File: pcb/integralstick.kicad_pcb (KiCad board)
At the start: 4 copper layers, 9 parts, among them J1 CONN_INTEGRALSTICK_FPGA_DEVICE, J2 CONN_INTEGRALSTICK_MCU_DEVICE, U1 STM32F777NIH6‎, U2 XC7A50T-1FTG256C, U3 S27KS0641, U4 S27KS0641, U5 KSZ9031RN, U6 S25FL064LABNFI011‎, U7 LTC3374-QFN

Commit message: Finished initial schematic. Pin assignments will likely change during routing. Ready for test point insertion and signoff review.
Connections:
- net Net-(U5-Pad1) renamed /Ethernet/A2V5
- net Net-(U5-Pad14) renamed /1V2
- net Net-(U5-Pad4) renamed /Ethernet/A1V2
- J1 pad 1: /Power Supply/1V8 -> /1V8
- J1 pad 100: /Power Supply/3V3 -> /3V3
- J1 pad 101: /FPGA/IO_3V3_18 -> /FPGA/IO_3V3_16
- J1 pad 102: /FPGA/IO_3V3_19 -> /FPGA/IO_3V3_17
- J1 pad 103: /FPGA/IO_3V3_20 -> /FPGA/IO_3V3_18
- J1 pad 104: /FPGA/IO_3V3_21 -> /FPGA/IO_3V3_19
- J1 pad 105: /Power Supply/3V3 -> /3V3
- J1 pad 106: /Power Supply/3V3 -> /3V3
- J1 pad 107: /FPGA/IO_3V3_22 -> /FPGA/IO_3V3_20
- J1 pad 108: /FPGA/IO_3V3_23 -> /FPGA/IO_3V3_21
- J1 pad 109: /FPGA/IO_3V3_24 -> /FPGA/IO_3V3_22
- J1 pad 110: /FPGA/IO_3V3_25 -> /FPGA/IO_3V3_23
- J1 pad 111: /Power Supply/3V3 -> /3V3
- J1 pad 112: /Power Supply/3V3 -> /3V3
- J1 pad 113: /FPGA/IO_3V3_26 -> /FPGA/IO_3V3_24
- J1 pad 114: /FPGA/IO_3V3_27 -> /FPGA/IO_3V3_25
- J1 pad 115: /FPGA/IO_3V3_28 -> /FPGA/IO_3V3_26
- J1 pad 116: /FPGA/IO_3V3_29 -> /FPGA/IO_3V3_27
- J1 pad 117: /Power Supply/3V3 -> /3V3
- J1 pad 118: /Power Supply/3V3 -> /3V3
- J1 pad 119: /FPGA/IO_3V3_30 -> /FPGA/IO_3V3_28
- J1 pad 120: /FPGA/IO_3V3_31 -> /FPGA/IO_3V3_29
- J1 pad 121: /Power Supply/GND -> /1V8
- J1 pad 122: /Power Supply/GND -> /1V8
- J1 pad 123: /Power Supply/GND -> /1V8
- J1 pad 124: /Power Supply/GND -> /1V8
- J1 pad 125: /Power Supply/GND -> /1V8
- J1 pad 126: /Power Supply/GND -> /1V8
- J1 pad 127: /Power Supply/GND -> /1V8
- J1 pad 128: /Power Supply/GND -> /1V8
- J1 pad 13: /Power Supply/1V8 -> /1V8
- J1 pad 14: /Power Supply/1V8 -> /1V8
- J1 pad 19: /Power Supply/1V8 -> /1V8
- J1 pad 2: /Power Supply/1V8 -> /1V8
- J1 pad 20: /Power Supply/1V8 -> /1V8
- J1 pad 25: /Power Supply/1V8 -> /1V8
- J1 pad 26: /Power Supply/1V8 -> /1V8
- J1 pad 31: /Power Supply/1V8 -> /1V8
- J1 pad 32: /Power Supply/1V8 -> /1V8
- J1 pad 69: /Power Supply/3V3 -> /3V3
- J1 pad 7: /Power Supply/1V8 -> /1V8
- J1 pad 70: /Power Supply/3V3 -> /3V3
- J1 pad 75: /Power Supply/3V3 -> /3V3
- J1 pad 76: /Power Supply/3V3 -> /3V3
- J1 pad 78: /FPGA/IO_3V3_3 -> /FPGA/IN_3V3_0_P
- J1 pad 79: /FPGA/IO_3V3_4 -> /FPGA/IO_3V3_3
- J1 pad 8: /Power Supply/1V8 -> /1V8
- J1 pad 80: /FPGA/IO_3V3_5 -> /FPGA/IN_3V3_0_N
- J1 pad 81: /Power Supply/3V3 -> /3V3
- J1 pad 82: /Power Supply/3V3 -> /3V3
- J1 pad 83: /FPGA/IO_3V3_6 -> /FPGA/IO_3V3_4
- J1 pad 84: /FPGA/IO_3V3_7 -> /FPGA/IO_3V3_5
- J1 pad 85: /FPGA/IO_3V3_8 -> /FPGA/IO_3V3_6
- J1 pad 86: /FPGA/IO_3V3_9 -> /FPGA/IO_3V3_7
- J1 pad 87: /Power Supply/3V3 -> /3V3
- J1 pad 88: /Power Supply/3V3 -> /3V3
- J1 pad 89: /FPGA/IO_3V3_10 -> /FPGA/IO_3V3_8
- J1 pad 90: /FPGA/IO_3V3_11 -> /FPGA/IO_3V3_9
- J1 pad 91: /FPGA/IO_3V3_12 -> /FPGA/IO_3V3_10
- J1 pad 92: /FPGA/IO_3V3_13 -> /FPGA/IO_3V3_11
- J1 pad 93: /Power Supply/3V3 -> /3V3
- J1 pad 94: /Power Supply/3V3 -> /3V3
- J1 pad 95: /FPGA/IO_3V3_14 -> /FPGA/IO_3V3_12
- J1 pad 96: /FPGA/IO_3V3_15 -> /FPGA/IO_3V3_13
- J1 pad 97: /FPGA/IO_3V3_16 -> /FPGA/IO_3V3_14
- J1 pad 98: /FPGA/IO_3V3_17 -> /FPGA/IO_3V3_15
- J1 pad 99: /Power Supply/3V3 -> /3V3
- J2 pad 1: (no net) -> /3V3
- J2 pad 10: (no net) -> /FPGA_RST_N
- J2 pad 103: (no net) -> /3V3
- J2 pad 104: (no net) -> /3V3
- J2 pad 109: /Power Supply/GND -> /1V8
- J2 pad 11: (no net) -> /FPGA_DONE
- J2 pad 110: /Power Supply/GND -> /1V8
- J2 pad 115: /Power Supply/GND -> /1V8
- J2 pad 116: /Power Supply/GND -> /1V8
- J2 pad 12: (no net) -> Net-(J2-Pad12)
- J2 pad 121: /Power Supply/GND -> /1V8
- J2 pad 122: /Power Supply/GND -> /1V8
- J2 pad 123: /Power Supply/GND -> /1V8
- J2 pad 124: /Power Supply/GND -> /1V8
- J2 pad 125: /Power Supply/GND -> /1V8
- J2 pad 126: /Power Supply/GND -> /1V8
- J2 pad 127: /Power Supply/GND -> /1V8
- J2 pad 128: /Power Supply/GND -> /1V8
- J2 pad 13: (no net) -> /3V3
- J2 pad 14: (no net) -> /3V3
- J2 pad 19: (no net) -> /3V3
- J2 pad 2: (no net) -> /3V3
- J2 pad 20: (no net) -> /3V3
- J2 pad 25: (no net) -> /3V3
- J2 pad 26: (no net) -> /3V3
- J2 pad 3: (no net) -> /FPGA_TDI
- J2 pad 31: (no net) -> /3V3
- J2 pad 32: (no net) -> /3V3
- J2 pad 37: (no net) -> /3V3
- J2 pad 38: (no net) -> /3V3
- J2 pad 4: (no net) -> /JTAG_TMS
- J2 pad 43: (no net) -> /3V3
- J2 pad 44: (no net) -> /3V3
- J2 pad 49: (no net) -> /3V3
- J2 pad 5: (no net) -> /JTAG_TCK
- J2 pad 50: (no net) -> /3V3
- J2 pad 55: (no net) -> /3V3
- J2 pad 56: (no net) -> /3V3
- J2 pad 6: (no net) -> /MCU_TDO
- J2 pad 61: (no net) -> /3V3
- J2 pad 62: (no net) -> /3V3
- J2 pad 67: (no net) -> /3V3
- J2 pad 68: (no net) -> /3V3
- J2 pad 7: (no net) -> /3V3
- J2 pad 73: (no net) -> /3V3
- J2 pad 74: (no net) -> /3V3
- J2 pad 79: (no net) -> /3V3
- J2 pad 8: (no net) -> /3V3
- J2 pad 80: (no net) -> /3V3
- J2 pad 85: (no net) -> /3V3
- J2 pad 86: (no net) -> /3V3
- J2 pad 9: (no net) -> /MCU_RST_N
- J2 pad 91: (no net) -> /3V3
- J2 pad 92: (no net) -> /3V3
- J2 pad 97: (no net) -> /3V3
- J2 pad 98: (no net) -> /3V3
- U1 pad A10: (no net) -> /MCU_TDO
- U1 pad A13: (no net) -> /FPGA_TDO
- U1 pad A14: (no net) -> /JTAG_TCK
- U1 pad A15: (no net) -> /JTAG_TMS
- U1 pad A4: (no net) -> Net-(U1-PadA4)
- U1 pad B10: (no net) -> Net-(U1-PadB10)
- U1 pad B3: (no net) -> Net-(U1-PadB3)
- U1 pad B7: (no net) -> Net-(U1-PadB7)
- U1 pad B8: (no net) -> Net-(U1-PadB8)
- U1 pad B9: (no net) -> Net-(U1-PadB9)
- U1 pad C1: (no net) -> /3V3
- U1 pad C13: (no net) -> Net-(U1-PadC13)
- U1 pad C14: (no net) -> Net-(U1-PadC14)
- U1 pad C2: (no net) -> Net-(U1-PadC2)
- U1 pad C3: (no net) -> Net-(U1-PadC3)
- U1 pad C4: (no net) -> Net-(U1-PadC4)
- U1 pad C5: (no net) -> Net-(U1-PadC5)
- U1 pad C6: (no net) -> Net-(U1-PadC6)
- U1 pad C7: (no net) -> Net-(U1-PadC7)
- U1 pad C8: (no net) -> Net-(U1-PadC8)
- U1 pad C9: (no net) -> Net-(U1-PadC9)
- U1 pad D10: (no net) -> Net-(U1-PadD10)
- U1 pad D13: (no net) -> Net-(U1-PadD13)
- U1 pad D14: (no net) -> Net-(U1-PadD14)
- U1 pad D3: (no net) -> Net-(U1-PadD3)
- U1 pad D4: (no net) -> Net-(U1-PadD4)
- U1 pad D5: (no net) -> Net-(U1-PadD5)
- U1 pad D6: (no net) -> Net-(U1-PadD6)
- U1 pad D7: (no net) -> Net-(U1-PadD7)
- U1 pad D8: (no net) -> Net-(U1-PadD8)
- U1 pad D9: (no net) -> Net-(U1-PadD9)
- U1 pad E1: (no net) -> /MCU/CLK_32KHZ
- U1 pad E10: /Power Supply/3V3 -> /3V3
- U1 pad E11: (no net) -> Net-(C2-Pad1)
- U1 pad E12: (no net) -> Net-(U1-PadE12)
- U1 pad E13: (no net) -> Net-(U1-PadE13)
- U1 pad E14: (no net) -> Net-(U1-PadE14)
- U1 pad E3: (no net) -> Net-(U1-PadE3)
- U1 pad E4: (no net) -> Net-(U1-PadE4)
- U1 pad E5: (no net) -> /3V3
- U1 pad E6: (no net) -> /1V8
- U1 pad E7: /Power Supply/3V3 -> /3V3
- U1 pad E8: /Power Supply/3V3 -> /3V3
- U1 pad E9: (no net) -> /3V3
- U1 pad F1: (no net) -> Net-(U1-PadF1)
- U1 pad F10: /Power Supply/GND -> /1V8
- U1 pad F11: /Power Supply/3V3 -> /3V3
- U1 pad F12: (no net) -> Net-(U1-PadF12)
- U1 pad F13: (no net) -> Net-(U1-PadF13)
- U1 pad F2: /Power Supply/GND -> /1V8
- U1 pad F3: (no net) -> Net-(U1-PadF3)
- U1 pad F4: /Power Supply/3V3 -> /3V3
- U1 pad F5: /Power Supply/3V3 -> /3V3
- U1 pad F6: /Power Supply/GND -> /1V8
- U1 pad F7: /Power Supply/GND -> /1V8
- U1 pad F8: /Power Supply/GND -> /1V8
- U1 pad F9: /Power Supply/GND -> /1V8
- U1 pad G1: (no net) -> /MCU/MCU_CLK_25MHZ
- U1 pad G10: /Power Supply/GND -> /1V8
- U1 pad G11: (no net) -> /3V3
- U1 pad G12: (no net) -> Net-(U1-PadG12)
- U1 pad G13: (no net) -> Net-(U1-PadG13)
- U1 pad G3: (no net) -> Net-(U1-PadG3)
- U1 pad G4: (no net) -> Net-(U1-PadG4)
- U1 pad G5: /Power Supply/3V3 -> /3V3
- U1 pad G6: /Power Supply/GND -> /1V8
- U1 pad H1: (no net) -> Net-(U1-PadH1)
- U1 pad H10: /Power Supply/GND -> /1V8
- U1 pad H11: /Power Supply/3V3 -> /3V3
- U1 pad H12: (no net) -> Net-(U1-PadH12)
- U1 pad H13: (no net) -> Net-(U1-PadH13)
- U1 pad H14: (no net) -> Net-(U1-PadH14)
- U1 pad H3: (no net) -> Net-(U1-PadH3)
- U1 pad H4: (no net) -> Net-(U1-PadH4)
- U1 pad H5: /Power Supply/3V3 -> /3V3
- U1 pad H6: /Power Supply/GND -> /1V8
- U1 pad J1: (no net) -> /MCU_RST_N
- U1 pad J10: /Power Supply/GND -> /1V8
- U1 pad J11: /Power Supply/3V3 -> /3V3
- U1 pad J12: (no net) -> Net-(U1-PadJ12)
- U1 pad J13: (no net) -> Net-(U1-PadJ13)
- U1 pad J14: (no net) -> Net-(U1-PadJ14)
- U1 pad J15: (no net) -> Net-(U1-PadJ15)
- U1 pad J3: (no net) -> Net-(U1-PadJ3)
- U1 pad J4: (no net) -> Net-(U1-PadJ4)
- U1 pad J5: /Power Supply/3V3 -> /3V3
- U1 pad J6: /Power Supply/GND -> /1V8
- U1 pad K10: /Power Supply/GND -> /1V8
- U1 pad K11: /Power Supply/3V3 -> /3V3
- U1 pad K12: (no net) -> Net-(U1-PadK12)
- U1 pad K4: (no net) -> Net-(U1-PadK4)
- U1 pad K5: /Power Supply/3V3 -> /3V3
- U1 pad K6: /Power Supply/GND -> /1V8
- U1 pad K7: /Power Supply/GND -> /1V8
- U1 pad K8: /Power Supply/GND -> /1V8
- U1 pad K9: /Power Supply/GND -> /1V8
- U1 pad L1: (no net) -> Net-(U1-PadL1)
- U1 pad L10: /Power Supply/3V3 -> /3V3
- U1 pad L11: (no net) -> Net-(C1-Pad2)
- U1 pad L5: (no net) -> /1V8
- U1 pad L6: /Power Supply/GND -> /1V8
- U1 pad L7: /Power Supply/3V3 -> /3V3
- U1 pad L8: /Power Supply/3V3 -> /3V3
- U1 pad L9: /Power Supply/3V3 -> /3V3
- U1 pad M1: /Power Supply/GND -> /1V8
- U1 pad M12: (no net) -> Net-(U1-PadM12)
- U1 pad M13: (no net) -> Net-(U1-PadM13)
- U1 pad M14: (no net) -> Net-(U1-PadM14)
- U1 pad M15: (no net) -> Net-(U1-PadM15)
- U1 pad M6: (no net) -> Net-(U1-PadM6)
- U1 pad M7: (no net) -> Net-(U1-PadM7)
- U1 pad M8: (no net) -> Net-(U1-PadM8)
- U1 pad M9: (no net) -> Net-(U1-PadM9)
- U1 pad N1: (no net) -> /1V8
- U1 pad N11: (no net) -> Net-(U1-PadN11)
- U1 pad N12: (no net) -> Net-(U1-PadN12)
- U1 pad N13: (no net) -> Net-(U1-PadN13)
- U1 pad N14: (no net) -> Net-(U1-PadN14)
- U1 pad N15: (no net) -> Net-(U1-PadN15)
- U1 pad N6: (no net) -> Net-(U1-PadN6)
- U1 pad N7: (no net) -> Net-(U1-PadN7)
- U1 pad N8: (no net) -> Net-(U1-PadN8)
- U1 pad P1: (no net) -> /3V3
- U1 pad P13: (no net) -> Net-(U1-PadP13)
- U1 pad P14: (no net) -> Net-(U1-PadP14)
- U1 pad P15: (no net) -> Net-(U1-PadP15)
- U1 pad P6: (no net) -> Net-(U1-PadP6)
- U1 pad P7: (no net) -> Net-(U1-PadP7)
- U1 pad P8: (no net) -> Net-(U1-PadP8)
- U1 pad R1: /Power Supply/3V3 -> /3V3
- U1 pad R6: (no net) -> Net-(U1-PadR6)
- U1 pad R7: (no net) -> Net-(U1-PadR7)
- U2 pad A1: /Power Supply/GND -> /1V8
- U2 pad A11: /Power Supply/GND -> /1V8
- U2 pad A16: /Power Supply/3V3 -> /3V3
- U2 pad A6: /Power Supply/1V8 -> /1V8
- U2 pad B13: /Power Supply/3V3 -> /3V3
- U2 pad B3: /Power Supply/1V8 -> /1V8
- U2 pad B8: /Power Supply/GND -> /1V8
- U2 pad C10: /Power Supply/3V3 -> /3V3
- U2 pad C15: /Power Supply/GND -> /1V8
- U2 pad C5: /Power Supply/GND -> /1V8
- U2 pad D12: /Power Supply/GND -> /1V8
- U2 pad D16: (no net) -> /FPGA/IN_3V3_0_N
- U2 pad D2: /Power Supply/GND -> /1V8
- U2 pad D7: /Power Supply/1V8 -> /1V8
- U2 pad E14: /Power Supply/3V3 -> /3V3
- U2 pad E15: (no net) -> Net-(U2-PadE15)
- U2 pad E16: /FPGA/IO_3V3_31 -> /FPGA/IN_3V3_0_P
- U2 pad E4: /Power Supply/1V8 -> /1V8
- U2 pad E7: (no net) -> /FPGA/3V3
- U2 pad E8: (no net) -> /QSPI_CLK
- U2 pad E9: /Power Supply/GND -> /1V8
- U2 pad F1: /Power Supply/1V8 -> /1V8
- U2 pad F10: /Power Supply/GND -> /1V8
- U2 pad F13: /FPGA/IO_3V3_30 -> Net-(U2-PadF13)
- U2 pad F14: (no net) -> Net-(U2-PadF14)
- U2 pad F15: (no net) -> Net-(U2-PadF15)
- U2 pad F16: /Power Supply/GND -> /1V8
- U2 pad F6: /Power Supply/GND -> /1V8
- U2 pad F8: (no net) -> /1V8
- U2 pad G10: Net-(U2-PadG10) -> /1V8
- U2 pad G11: (no net) -> Net-(U2-PadG11)
- U2 pad G12: (no net) -> Net-(U2-PadG12)
- U2 pad G13: /Power Supply/GND -> /1V8
- U2 pad G14: (no net) -> Net-(U2-PadG14)
- U2 pad G15: (no net) -> /FPGA/I2C_SDA
- U2 pad G16: (no net) -> Net-(U2-PadG16)
- U2 pad G3: /Power Supply/GND -> /1V8
- U2 pad G7: /Power Supply/GND -> /1V8
- U2 pad G8: (no net) -> /1V8
- U2 pad G9: /Power Supply/GND -> /1V8
- U2 pad H10: (no net) -> /FPGA_DONE
- U2 pad H11: (no net) -> Net-(U2-PadH11)
- U2 pad H12: (no net) -> Net-(U2-PadH12)
- U2 pad H13: (no net) -> Net-(U2-PadH13)
- U2 pad H14: (no net) -> /FPGA/I2C_SCL
- U2 pad H15: /Power Supply/3V3 -> /3V3
- U2 pad H16: (no net) -> Net-(U2-PadH16)
- U2 pad H6: /Power Supply/GND -> /1V8
- U2 pad H7: (no net) -> /FPGA/GND
- U2 pad H8: (no net) -> Net-(U2-PadH8)
- U2 pad J10: Net-(U2-PadG10) -> /1V8
- U2 pad J11: /Power Supply/GND -> /1V8
- U2 pad J12: /Power Supply/3V3 -> /3V3
- U2 pad J15: (no net) -> Net-(U2-PadJ15)
- U2 pad J16: (no net) -> Net-(U2-PadJ16)
- U2 pad J2: /Power Supply/1V8 -> /1V8
- U2 pad J7: (no net) -> Net-(U2-PadJ7)
- U2 pad J8: (no net) -> /FPGA/GND
- U2 pad J9: /Power Supply/GND -> /1V8
- U2 pad K10: (no net) -> /FPGA/FPGA_INIT
- U2 pad K11: Net-(U2-PadG10) -> /1V8
- U2 pad K12: (no net) -> Net-(U2-PadK12)
- U2 pad K14: /Power Supply/GND -> /1V8
- U2 pad K4: /Power Supply/GND -> /1V8
- U2 pad K6: /Power Supply/GND -> /1V8
- U2 pad K7: (no net) -> /FPGA/GND
- U2 pad K8: (no net) -> /FPGA/GND
- U2 pad L1: /Power Supply/GND -> /1V8
- U2 pad L10: Net-(U2-PadG10) -> /1V8
- U2 pad L11: /Power Supply/GND -> /1V8
- U2 pad L15: /MCU/3V3 -> /3V3
- U2 pad L16: /Power Supply/3V3 -> /3V3
- U2 pad L6: /Power Supply/3V3 -> /3V3
- U2 pad L7: (no net) -> /JTAG_TCK
- U2 pad L9: (no net) -> /FPGA_RST_N
- U2 pad M10: (no net) -> /FPGA/GND
- U2 pad M11: (no net) -> /FPGA/GND
- U2 pad M13: /Power Supply/3V3 -> /3V3
- U2 pad M7: (no net) -> /JTAG_TMS
- U2 pad M8: /Power Supply/GND -> /1V8
- U2 pad M9: (no net) -> /FPGA/3V3
- U2 pad N10: /Power Supply/3V3 -> /3V3
- U2 pad N15: /Power Supply/GND -> /1V8
- U2 pad N5: /Power Supply/GND -> /1V8
- U2 pad N7: (no net) -> /FPGA_TDI
- U2 pad N8: (no net) -> /FPGA_TDO
- U2 pad N9: (no net) -> Net-(U2-PadN9)
- U2 pad P11: (no net) -> /ETH_LED1_N
- U2 pad P12: /Power Supply/GND -> /1V8
- U2 pad P2: /Power Supply/GND -> /1V8
- U2 pad P7: /Power Supply/3V3 -> /3V3
- U2 pad R10: (no net) -> Net-(U2-PadR10)
- U2 pad R11: (no net) -> Net-(U2-PadR11)
- U2 pad R12: (no net) -> /ETH_LED2_N
- U2 pad R13: (no net) -> Net-(U2-PadR13)
- U2 pad R14: /Power Supply/3V3 -> /3V3
- U2 pad R9: /Power Supply/GND -> /1V8
- U2 pad T11: /Power Supply/3V3 -> /3V3
- U2 pad T12: (no net) -> Net-(U2-PadT12)
- U2 pad T13: (no net) -> Net-(U2-PadT13)
- U2 pad T16: /Power Supply/GND -> /1V8
- U2 pad T6: /Power Supply/GND -> /1V8
- U3 pad B3: /RAM/GND -> /1V8
- U3 pad B4: /RAM/1V8 -> /1V8
- U3 pad C1: /RAM/GND -> /1V8
- U3 pad D1: /RAM/1V8 -> /1V8
- U3 pad E4: /RAM/1V8 -> /1V8
- U3 pad E5: /RAM/GND -> /1V8
- U4 pad B3: /RAM/GND -> /1V8
- U4 pad B4: /RAM/1V8 -> /1V8
- U4 pad C1: /RAM/GND -> /1V8
- U4 pad D1: /RAM/1V8 -> /1V8
- U4 pad E4: /RAM/1V8 -> /1V8
- U4 pad E5: /RAM/GND -> /1V8
- U5 pad 13: (no net) -> Net-(U5-Pad13)
- U5 pad 15: (no net) -> /ETH_LED2_N
- U5 pad 16: Net-(U5-Pad16) -> /3V3
- U5 pad 17: (no net) -> /ETH_LED1_N
- U5 pad 29: Net-(U5-Pad29) -> /1V8
- U5 pad 34: Net-(U5-Pad16) -> /3V3
- U5 pad 38: (no net) -> Net-(U5-Pad38)
- U5 pad 40: Net-(U5-Pad16) -> /3V3
- U5 pad 41: (no net) -> Net-(R5-Pad2)
- U5 pad 43: (no net) -> Net-(U5-Pad43)
- U5 pad 44: (no net) -> /Ethernet/A1V2_PLL
- U5 pad 45: (no net) -> Net-(U5-Pad45)
- U5 pad 46: (no net) -> /Ethernet/ETH_CLK_25MHZ
- U5 pad 47: (no net) -> Net-(U5-Pad47)
- U5 pad 48: (no net) -> Net-(R2-Pad2)
- U5 pad PAD: Net-(U5-Pad29) -> /1V8
- U6 pad 4: (no net) -> /1V8
- U6 pad 6: (no net) -> /QSPI_CLK
- U6 pad 8: /MCU/3V3 -> /3V3
- U7 pad 1: (no net) -> Net-(U7-Pad1)
- U7 pad 10: (no net) -> Net-(U7-Pad10)
- U7 pad 11: (no net) -> Net-(U7-Pad11)
- U7 pad 12: (no net) -> Net-(U7-Pad12)
- U7 pad 13: (no net) -> Net-(U7-Pad13)
- U7 pad 14: (no net) -> Net-(U7-Pad14)
- U7 pad 15: (no net) -> Net-(U7-Pad15)
- U7 pad 16: (no net) -> Net-(U7-Pad16)
- U7 pad 17: (no net) -> Net-(U7-Pad17)
- U7 pad 18: (no net) -> Net-(U7-Pad18)
- U7 pad 19: (no net) -> Net-(U7-Pad19)
- U7 pad 2: (no net) -> Net-(U7-Pad2)
- U7 pad 20: (no net) -> Net-(U7-Pad20)
- U7 pad 21: (no net) -> Net-(U7-Pad21)
- U7 pad 22: (no net) -> Net-(U7-Pad22)
- U7 pad 23: (no net) -> Net-(U7-Pad23)
- U7 pad 24: (no net) -> Net-(U7-Pad24)
- U7 pad 25: (no net) -> Net-(U7-Pad25)
- U7 pad 26: (no net) -> Net-(U7-Pad26)
- U7 pad 27: (no net) -> Net-(U7-Pad27)
- U7 pad 28: (no net) -> Net-(U7-Pad28)
- U7 pad 29: (no net) -> Net-(U7-Pad29)
- U7 pad 3: (no net) -> Net-(U7-Pad3)
- U7 pad 30: (no net) -> Net-(U7-Pad30)
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
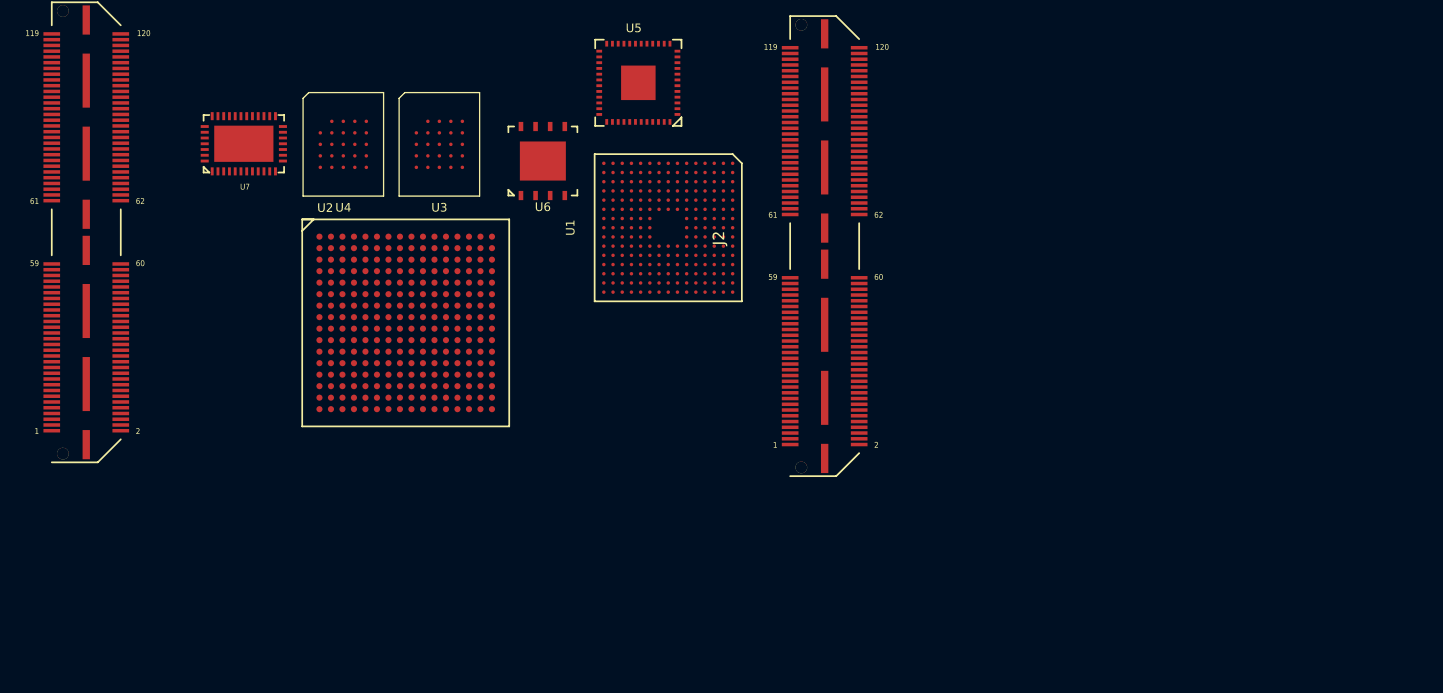
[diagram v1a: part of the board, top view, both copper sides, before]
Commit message: Assigned lots of footprints. Still have a few to go.
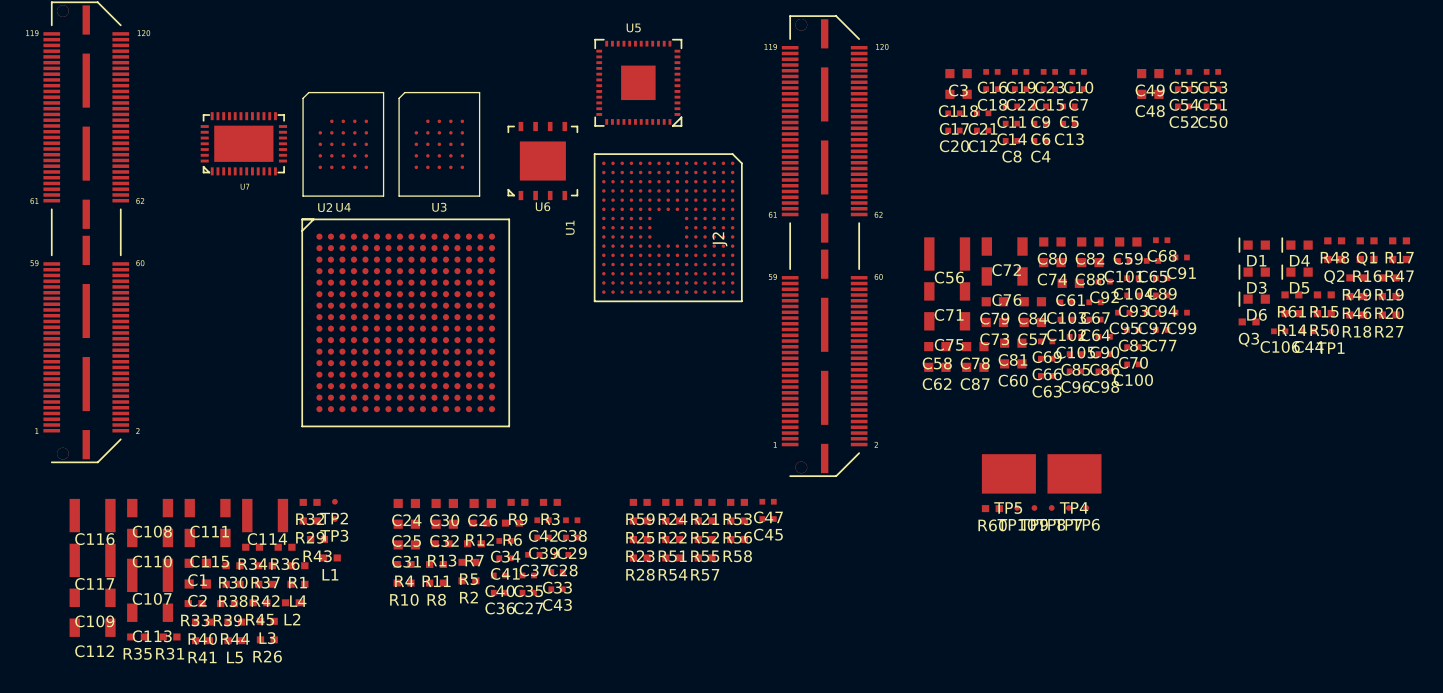
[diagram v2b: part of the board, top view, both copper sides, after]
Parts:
- added C1: 2.2 uF, azonenberg_pcb:EIA_0603_CAP_NOSILK, F.Cu at (37.5, 73.0)
- added C10: 0.47 uF, azonenberg_pcb:EIA_0402_CAP_NOSILK, F.Cu at (114.0, 30.2)
- added C100: 0.47 uF, azonenberg_pcb:EIA_0402_CAP_NOSILK, F.Cu at (118.8, 55.7)
- added C101: 0.47 uF, azonenberg_pcb:EIA_0402_CAP_NOSILK, F.Cu at (118.0, 46.7)
- added C102: 0.47 uF, azonenberg_pcb:EIA_0402_CAP_NOSILK, F.Cu at (113.0, 51.8)
- added C103: 0.47 uF, azonenberg_pcb:EIA_0402_CAP_NOSILK, F.Cu at (113.0, 50.3)
- added C104: 0.47 uF, azonenberg_pcb:EIA_0402_CAP_NOSILK, F.Cu at (118.8, 48.2)
- added C105: 0.47 uF, azonenberg_pcb:EIA_0402_CAP_NOSILK, F.Cu at (113.8, 53.3)
- added C106: 0.47 uF, azonenberg_pcb:EIA_0402_CAP_NOSILK, F.Cu at (131.6, 52.8)
- added C107: 47 uF, azonenberg_pcb:EIA_1210_CAP_NOSILK, F.Cu at (33.4, 74.0)
- added C108: 22 uF, azonenberg_pcb:EIA_1206_CAP_NOSILK, F.Cu at (33.4, 68.2)
- added C109: 22 uF, azonenberg_pcb:EIA_1206_CAP_NOSILK, F.Cu at (28.4, 76.0)
- added C11: 0.47 uF, azonenberg_pcb:EIA_0402_CAP_NOSILK, F.Cu at (108.2, 33.2)
- added C110: 22 uF, azonenberg_pcb:EIA_1206_CAP_NOSILK, F.Cu at (33.4, 70.8)
- added C111: 10 uF, azonenberg_pcb:EIA_1206_CAP_NOSILK, F.Cu at (38.4, 68.2)
- added C112: 22 uF, azonenberg_pcb:EIA_1206_CAP_NOSILK, F.Cu at (28.4, 78.6)
- added C113: 10 uF, azonenberg_pcb:EIA_1206_CAP_NOSILK, F.Cu at (33.4, 77.3)
- added C114: 47 uF, azonenberg_pcb:EIA_1210_CAP_NOSILK, F.Cu at (43.4, 68.8)
- added C115: 10 uF, azonenberg_pcb:EIA_1206_CAP_NOSILK, F.Cu at (38.4, 70.8)
- added C116: 100 uF, azonenberg_pcb:EIA_1210_CAP_NOSILK, F.Cu at (28.4, 68.8)
- added C117: 47 uF, azonenberg_pcb:EIA_1210_CAP_NOSILK, F.Cu at (28.4, 72.7)
- added C118: 4.7 uF, azonenberg_pcb:EIA_0603_CAP_NOSILK, F.Cu at (103.6, 32.2)
- added C12: 0.47 uF, azonenberg_pcb:EIA_0402_CAP_NOSILK, F.Cu at (105.7, 35.4)
- added C13: 0.47 uF, azonenberg_pcb:EIA_0402_CAP_NOSILK, F.Cu at (113.2, 34.8)
- added C14: 0.47 uF, azonenberg_pcb:EIA_0402_CAP_NOSILK, F.Cu at (108.2, 34.8)
- added C15: 0.47 uF, azonenberg_pcb:EIA_0402_CAP_NOSILK, F.Cu at (111.5, 31.8)
- added C16: 0.47 uF, azonenberg_pcb:EIA_0402_CAP_NOSILK, F.Cu at (106.5, 30.2)
- added C17: 0.47 uF, azonenberg_pcb:EIA_0402_CAP_NOSILK, F.Cu at (103.2, 33.9)
- added C18: 0.47 uF, azonenberg_pcb:EIA_0402_CAP_NOSILK, F.Cu at (106.5, 31.8)
- added C19: 0.47 uF, azonenberg_pcb:EIA_0402_CAP_NOSILK, F.Cu at (109.0, 30.2)
- added C2: 2.2 uF, azonenberg_pcb:EIA_0603_CAP_NOSILK, F.Cu at (37.5, 74.8)
- added C20: 0.47 uF, azonenberg_pcb:EIA_0402_CAP_NOSILK, F.Cu at (103.2, 35.4)
- added C21: 0.47 uF, azonenberg_pcb:EIA_0402_CAP_NOSILK, F.Cu at (105.7, 33.9)
- added C22: 0.47 uF, azonenberg_pcb:EIA_0402_CAP_NOSILK, F.Cu at (109.0, 31.8)
- added C23: 0.47 uF, azonenberg_pcb:EIA_0402_CAP_NOSILK, F.Cu at (111.5, 30.2)
- added C24: 4.7 uF, azonenberg_pcb:EIA_0603_CAP_NOSILK, F.Cu at (55.7, 67.8)
- added C25: 4.7 uF, azonenberg_pcb:EIA_0603_CAP_NOSILK, F.Cu at (55.7, 69.6)
- added C26: 4.7 uF, azonenberg_pcb:EIA_0603_CAP_NOSILK, F.Cu at (62.3, 67.8)
- added C27: 0.47 uF, azonenberg_pcb:EIA_0402_CAP_NOSILK, F.Cu at (66.2, 75.5)
- added C28: 0.47 uF, azonenberg_pcb:EIA_0402_CAP_NOSILK, F.Cu at (69.2, 72.2)
- added C29: 0.47 uF, azonenberg_pcb:EIA_0402_CAP_NOSILK, F.Cu at (70.0, 70.7)
- added C3: 4.7 uF, azonenberg_pcb:EIA_0603_CAP_NOSILK, F.Cu at (103.6, 30.4)
- added C30: 4.7 uF, azonenberg_pcb:EIA_0603_CAP_NOSILK, F.Cu at (59.0, 67.8)
- added C31: 4.7 uF, azonenberg_pcb:EIA_0603_CAP_NOSILK, F.Cu at (55.7, 71.4)
- added C32: 4.7 uF, azonenberg_pcb:EIA_0603_CAP_NOSILK, F.Cu at (59.0, 69.6)
- added C33: 0.47 uF, azonenberg_pcb:EIA_0402_CAP_NOSILK, F.Cu at (68.7, 73.7)
- added C34: 0.47 uF, azonenberg_pcb:EIA_0402_CAP_NOSILK, F.Cu at (64.2, 71.0)
- added C35: 0.47 uF, azonenberg_pcb:EIA_0402_CAP_NOSILK, F.Cu at (66.2, 74.0)
- added C36: 0.47 uF, azonenberg_pcb:EIA_0402_CAP_NOSILK, F.Cu at (63.7, 75.5)
- added C37: 0.47 uF, azonenberg_pcb:EIA_0402_CAP_NOSILK, F.Cu at (66.7, 72.2)
- added C38: 0.47 uF, azonenberg_pcb:EIA_0402_CAP_NOSILK, F.Cu at (70.0, 69.2)
- added C39: 0.47 uF, azonenberg_pcb:EIA_0402_CAP_NOSILK, F.Cu at (67.5, 70.7)
- added C4: 0.47 uF, azonenberg_pcb:EIA_0402_CAP_NOSILK, F.Cu at (110.7, 36.2)
- added C40: 0.47 uF, azonenberg_pcb:EIA_0402_CAP_NOSILK, F.Cu at (63.7, 74.0)
- added C41: 0.47 uF, azonenberg_pcb:EIA_0402_CAP_NOSILK, F.Cu at (64.2, 72.5)
- added C42: 0.47 uF, azonenberg_pcb:EIA_0402_CAP_NOSILK, F.Cu at (67.5, 69.2)
- added C43: 0.47 uF, azonenberg_pcb:EIA_0402_CAP_NOSILK, F.Cu at (68.7, 75.2)
- added C44: 0.47 uF, azonenberg_pcb:EIA_0402_CAP_NOSILK, F.Cu at (134.1, 52.8)
- added C45: 0.47 uF, azonenberg_pcb:EIA_0402_CAP_NOSILK, F.Cu at (87.1, 69.1)
- added C47: 0.47 uF, azonenberg_pcb:EIA_0402_CAP_NOSILK, F.Cu at (87.1, 67.6)
- added C48: 4.7 uF, azonenberg_pcb:EIA_0603_CAP_NOSILK, F.Cu at (120.3, 32.2)
- added C49: 4.7 uF, azonenberg_pcb:EIA_0603_CAP_NOSILK, F.Cu at (120.3, 30.4)
- added C5: 0.47 uF, azonenberg_pcb:EIA_0402_CAP_NOSILK, F.Cu at (113.2, 33.2)
- added C50: 0.47 uF, azonenberg_pcb:EIA_0402_CAP_NOSILK, F.Cu at (125.7, 33.2)
- added C51: 0.47 uF, azonenberg_pcb:EIA_0402_CAP_NOSILK, F.Cu at (125.7, 31.8)
- added C52: 0.47 uF, azonenberg_pcb:EIA_0402_CAP_NOSILK, F.Cu at (123.2, 33.2)
- added C53: 0.47 uF, azonenberg_pcb:EIA_0402_CAP_NOSILK, F.Cu at (125.7, 30.2)
- added C54: 0.47 uF, azonenberg_pcb:EIA_0402_CAP_NOSILK, F.Cu at (123.2, 31.8)
- added C55: 0.47 uF, azonenberg_pcb:EIA_0402_CAP_NOSILK, F.Cu at (123.2, 30.2)
- added C56: 330 uF, azonenberg_pcb:EIA_1210_CAP_NOSILK, F.Cu at (102.7, 46.1)
- added C57: 4.7 uF, azonenberg_pcb:EIA_0603_CAP_NOSILK, F.Cu at (110.1, 52.0)
- added C58: 4.7 uF, azonenberg_pcb:EIA_0603_CAP_NOSILK, F.Cu at (101.8, 54.1)
- added C59: 4.7 uF, azonenberg_pcb:EIA_0603_CAP_NOSILK, F.Cu at (118.4, 45.0)
- added C6: 0.47 uF, azonenberg_pcb:EIA_0402_CAP_NOSILK, F.Cu at (110.7, 34.8)
- added C60: 4.7 uF, azonenberg_pcb:EIA_0603_CAP_NOSILK, F.Cu at (108.4, 55.6)
- added C61: 4.7 uF, azonenberg_pcb:EIA_0603_CAP_NOSILK, F.Cu at (113.4, 48.6)
- added C62: 4.7 uF, azonenberg_pcb:EIA_0603_CAP_NOSILK, F.Cu at (101.8, 55.9)
- added C63: 0.47 uF, azonenberg_pcb:EIA_0402_CAP_NOSILK, F.Cu at (111.3, 56.7)
- added C64: 0.47 uF, azonenberg_pcb:EIA_0402_CAP_NOSILK, F.Cu at (115.5, 51.8)
- added C65: 0.47 uF, azonenberg_pcb:EIA_0402_CAP_NOSILK, F.Cu at (120.5, 46.7)
- added C66: 0.47 uF, azonenberg_pcb:EIA_0402_CAP_NOSILK, F.Cu at (111.3, 55.2)
- added C67: 0.47 uF, azonenberg_pcb:EIA_0402_CAP_NOSILK, F.Cu at (115.5, 50.3)
- added C68: 0.47 uF, azonenberg_pcb:EIA_0402_CAP_NOSILK, F.Cu at (121.3, 44.9)
- added C69: 0.47 uF, azonenberg_pcb:EIA_0402_CAP_NOSILK, F.Cu at (111.3, 53.7)
- added C7: 0.47 uF, azonenberg_pcb:EIA_0402_CAP_NOSILK, F.Cu at (114.0, 31.8)
- added C70: 0.47 uF, azonenberg_pcb:EIA_0402_CAP_NOSILK, F.Cu at (118.8, 54.2)
- added C71: 47 uF, azonenberg_pcb:EIA_1206_CAP_NOSILK, F.Cu at (102.7, 49.3)
- added C72: 100 uF, azonenberg_pcb:EIA_1206_CAP_NOSILK, F.Cu at (107.7, 45.4)
- added C73: 4.7 uF, azonenberg_pcb:EIA_0603_CAP_NOSILK, F.Cu at (106.8, 52.0)
- added C74: 4.7 uF, azonenberg_pcb:EIA_0603_CAP_NOSILK, F.Cu at (111.8, 46.8)
- added C75: 47 uF, azonenberg_pcb:EIA_1206_CAP_NOSILK, F.Cu at (102.7, 51.9)
- added C76: 47 uF, azonenberg_pcb:EIA_1206_CAP_NOSILK, F.Cu at (107.7, 48.0)
- added C77: 0.47 uF, azonenberg_pcb:EIA_0402_CAP_NOSILK, F.Cu at (121.3, 52.7)
- added C78: 4.7 uF, azonenberg_pcb:EIA_0603_CAP_NOSILK, F.Cu at (105.1, 54.1)
- added C79: 4.7 uF, azonenberg_pcb:EIA_0603_CAP_NOSILK, F.Cu at (106.8, 50.2)
- added C8: 0.47 uF, azonenberg_pcb:EIA_0402_CAP_NOSILK, F.Cu at (108.2, 36.2)
- added C80: 4.7 uF, azonenberg_pcb:EIA_0603_CAP_NOSILK, F.Cu at (111.8, 45.0)
- added C81: 4.7 uF, azonenberg_pcb:EIA_0603_CAP_NOSILK, F.Cu at (108.4, 53.8)
- added C82: 4.7 uF, azonenberg_pcb:EIA_0603_CAP_NOSILK, F.Cu at (115.1, 45.0)
- added C83: 0.47 uF, azonenberg_pcb:EIA_0402_CAP_NOSILK, F.Cu at (118.8, 52.7)
- added C84: 4.7 uF, azonenberg_pcb:EIA_0603_CAP_NOSILK, F.Cu at (110.1, 50.2)
- added C85: 0.47 uF, azonenberg_pcb:EIA_0402_CAP_NOSILK, F.Cu at (113.8, 54.8)
- added C86: 0.47 uF, azonenberg_pcb:EIA_0402_CAP_NOSILK, F.Cu at (116.3, 54.8)
- added C87: 4.7 uF, azonenberg_pcb:EIA_0603_CAP_NOSILK, F.Cu at (105.1, 55.9)
- added C88: 4.7 uF, azonenberg_pcb:EIA_0603_CAP_NOSILK, F.Cu at (115.1, 46.8)
- added C89: 0.47 uF, azonenberg_pcb:EIA_0402_CAP_NOSILK, F.Cu at (121.3, 48.2)
- added C9: 0.47 uF, azonenberg_pcb:EIA_0402_CAP_NOSILK, F.Cu at (110.7, 33.2)
- added C90: 0.47 uF, azonenberg_pcb:EIA_0402_CAP_NOSILK, F.Cu at (116.3, 53.3)
- added C91: 0.47 uF, azonenberg_pcb:EIA_0402_CAP_NOSILK, F.Cu at (123.0, 46.4)
- added C92: 0.47 uF, azonenberg_pcb:EIA_0402_CAP_NOSILK, F.Cu at (116.3, 48.5)
- added C93: 0.47 uF, azonenberg_pcb:EIA_0402_CAP_NOSILK, F.Cu at (118.8, 49.7)
- added C94: 0.47 uF, azonenberg_pcb:EIA_0402_CAP_NOSILK, F.Cu at (121.3, 49.7)
- added C95: 0.47 uF, azonenberg_pcb:EIA_0402_CAP_NOSILK, F.Cu at (118.0, 51.2)
- added C96: 0.47 uF, azonenberg_pcb:EIA_0402_CAP_NOSILK, F.Cu at (113.8, 56.3)
- added C97: 0.47 uF, azonenberg_pcb:EIA_0402_CAP_NOSILK, F.Cu at (120.5, 51.2)
- added C98: 0.47 uF, azonenberg_pcb:EIA_0402_CAP_NOSILK, F.Cu at (116.3, 56.3)
- added C99: 0.47 uF, azonenberg_pcb:EIA_0402_CAP_NOSILK, F.Cu at (123.0, 51.2)
- added D1: GREEN, azonenberg_pcb:EIA_0603_LED, F.Cu at (129.6, 45.3)
- added D3: GREEN, azonenberg_pcb:EIA_0603_LED, F.Cu at (129.6, 47.7)
- added D4: GREEN, azonenberg_pcb:EIA_0603_LED, F.Cu at (133.3, 45.3)
- added D5: GREEN, azonenberg_pcb:EIA_0603_LED, F.Cu at (133.3, 47.7)
- added D6: GREEN, azonenberg_pcb:EIA_0603_LED, F.Cu at (129.6, 50.0)
- added L1: SPM6530T-2R2M, azonenberg_pcb:EIA_0402_RES_NOSILK, F.Cu at (49.0, 72.5)
- added L2: NR6028T2R2N, azonenberg_pcb:EIA_0402_RES_NOSILK, F.Cu at (45.7, 76.4)
- added L3: NRS5030T2R2NMGJ, azonenberg_pcb:EIA_0402_RES_NOSILK, F.Cu at (43.5, 78.0)
- added L4: NRS5030T2R2NMGJ, azonenberg_pcb:EIA_0402_RES_NOSILK, F.Cu at (46.2, 74.8)
- added L5: NRS5030T2R2NMGJ, azonenberg_pcb:EIA_0402_RES_NOSILK, F.Cu at (40.7, 79.7)
- added Q1: SSM6N58NU, azonenberg_pcb:EIA_0402_RES_NOSILK, F.Cu at (139.2, 44.9)
- added Q2: SSM6N58NU, azonenberg_pcb:EIA_0402_RES_NOSILK, F.Cu at (136.3, 46.5)
- added Q3: SSM6N58NU, azonenberg_pcb:EIA_0402_RES_NOSILK, F.Cu at (128.9, 52.0)
- added R1: 10K, azonenberg_pcb:EIA_0402_RES_NOSILK, F.Cu at (46.2, 73.2)
- added R10: 10K, azonenberg_pcb:EIA_0402_RES_NOSILK, F.Cu at (55.4, 74.7)
- added R11: 10K, azonenberg_pcb:EIA_0402_RES_NOSILK, F.Cu at (58.3, 73.1)
- added R12: 10K, azonenberg_pcb:EIA_0402_RES_NOSILK, F.Cu at (62.0, 69.5)
- added R13: 10K, azonenberg_pcb:EIA_0402_RES_NOSILK, F.Cu at (58.7, 71.3)
- added R14: 4.7k, azonenberg_pcb:EIA_0402_RES_NOSILK, F.Cu at (132.6, 51.2)
- added R15: 4.7k, azonenberg_pcb:EIA_0402_RES_NOSILK, F.Cu at (135.4, 49.6)
- added R16: 100, azonenberg_pcb:EIA_0402_RES_NOSILK, F.Cu at (139.2, 46.5)
- added R17: 470, azonenberg_pcb:EIA_0402_RES_NOSILK, F.Cu at (142.0, 44.9)
- added R18: 1K, azonenberg_pcb:EIA_0402_RES_NOSILK, F.Cu at (138.3, 51.4)
- added R19: 4.7k, azonenberg_pcb:EIA_0402_RES_NOSILK, F.Cu at (141.1, 48.2)
- added R2: 12.1K 1%, azonenberg_pcb:EIA_0402_RES_NOSILK, F.Cu at (61.1, 74.5)
- added R20: 4.7k, azonenberg_pcb:EIA_0402_RES_NOSILK, F.Cu at (141.1, 49.8)
- added R21: 33, azonenberg_pcb:EIA_0402_RES_NOSILK, F.Cu at (81.6, 67.7)
- added R22: 33, azonenberg_pcb:EIA_0402_RES_NOSILK, F.Cu at (78.8, 69.3)
- added R23: 4.7k, azonenberg_pcb:EIA_0402_RES_NOSILK, F.Cu at (76.0, 70.9)
- added R24: 4.7k, azonenberg_pcb:EIA_0402_RES_NOSILK, F.Cu at (78.8, 67.7)
- added R25: 4.7k, azonenberg_pcb:EIA_0402_RES_NOSILK, F.Cu at (76.0, 69.3)
- added R26: 1K, azonenberg_pcb:EIA_0402_RES_NOSILK, F.Cu at (43.5, 79.6)
- added R27: 33, azonenberg_pcb:EIA_0402_RES_NOSILK, F.Cu at (141.1, 51.4)
- added R28: 0, azonenberg_pcb:EIA_0402_RES_NOSILK, F.Cu at (76.0, 72.5)
- added R29: 0, azonenberg_pcb:EIA_0402_RES_NOSILK, F.Cu at (47.3, 69.3)
- added R3: 1K, azonenberg_pcb:EIA_0402_RES_NOSILK, F.Cu at (68.2, 67.7)
- added R30: 0, azonenberg_pcb:EIA_0402_RES_NOSILK, F.Cu at (40.6, 73.2)
- added R31: 0, azonenberg_pcb:EIA_0402_RES_NOSILK, F.Cu at (35.1, 79.4)
- added R32: 0, azonenberg_pcb:EIA_0402_RES_NOSILK, F.Cu at (47.3, 67.7)
- added R33: 0, azonenberg_pcb:EIA_0402_RES_NOSILK, F.Cu at (37.3, 76.5)
- added R34: 255K, azonenberg_pcb:EIA_0402_RES_NOSILK, F.Cu at (42.3, 71.6)
- added R35: 232K, azonenberg_pcb:EIA_0402_RES_NOSILK, F.Cu at (32.3, 79.4)
- added R36: 806K, azonenberg_pcb:EIA_0402_RES_NOSILK, F.Cu at (45.1, 71.6)
- added R37: 1.02M, azonenberg_pcb:EIA_0402_RES_NOSILK, F.Cu at (43.4, 73.2)
- added R38: 1.02M, azonenberg_pcb:EIA_0402_RES_NOSILK, F.Cu at (40.6, 74.8)
- added R39: 1.02M, azonenberg_pcb:EIA_0402_RES_NOSILK, F.Cu at (40.1, 76.5)
- added R4: 1K, azonenberg_pcb:EIA_0402_RES_NOSILK, F.Cu at (55.4, 73.1)
- added R40: 464K, azonenberg_pcb:EIA_0402_RES_NOSILK, F.Cu at (37.9, 78.1)
- added R41: 649K, azonenberg_pcb:EIA_0402_RES_NOSILK, F.Cu at (37.9, 79.7)
- added R42: 475K, azonenberg_pcb:EIA_0402_RES_NOSILK, F.Cu at (43.4, 74.8)
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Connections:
- net /Power Supply/1V0 renamed /1V0
- net /Power Supply/2V5 renamed /2V5
- net Net-(U2-PadE15) renamed /FPGA/GPIO_LED0
- net Net-(U2-PadG12) renamed /FPGA/GPIO_LED2
- net Net-(U2-PadH11) renamed /FPGA/GPIO_LED1
- net Net-(U2-PadH12) renamed /FPGA/GPIO_LED3
- J1 pad 121: /1V8 -> /GND
- J1 pad 122: /1V8 -> /GND
- J1 pad 123: /1V8 -> /GND
- J1 pad 124: /1V8 -> /GND
- J1 pad 125: /1V8 -> /GND
- J1 pad 126: /1V8 -> /GND
- J1 pad 127: /1V8 -> /GND
- J1 pad 128: /1V8 -> /GND
- J2 pad 109: /1V8 -> /GND
- J2 pad 110: /1V8 -> /GND
- J2 pad 115: /1V8 -> /GND
- J2 pad 116: /1V8 -> /GND
- J2 pad 12: Net-(J2-Pad12) -> /MCU_BOOT0
- J2 pad 121: /1V8 -> /GND
- J2 pad 122: /1V8 -> /GND
- J2 pad 123: /1V8 -> /GND
- J2 pad 124: /1V8 -> /GND
- J2 pad 125: /1V8 -> /GND
- J2 pad 126: /1V8 -> /GND
- J2 pad 127: /1V8 -> /GND
- J2 pad 128: /1V8 -> /GND
- U1 pad A10: /MCU_TDO -> /MCU/JTAG_TDO
- U1 pad A4: Net-(U1-PadA4) -> /MCU/UART6_TX
- U1 pad C1: /3V3 -> /Power Supply/MCU_VBAT
- U1 pad D9: Net-(U1-PadD9) -> /MCU/UART6_RX
- U1 pad E6: /1V8 -> /MCU_BOOT0
- U1 pad F10: /1V8 -> /GND
- U1 pad F2: /1V8 -> /GND
- U1 pad F6: /1V8 -> /GND
- U1 pad F7: /1V8 -> /GND
- U1 pad F8: /1V8 -> /GND
- U1 pad F9: /1V8 -> /GND
- U1 pad G1: /MCU/MCU_CLK_25MHZ -> /MCU/MCU_CLK
- U1 pad G10: /1V8 -> /GND
- U1 pad G6: /1V8 -> /GND
- U1 pad H10: /1V8 -> /GND
- U1 pad H6: /1V8 -> /GND
- U1 pad J10: /1V8 -> /GND
- U1 pad J3: Net-(U1-PadJ3) -> /MCU/SPI5_CS_N
- U1 pad J6: /1V8 -> /GND
- U1 pad K10: /1V8 -> /GND
- U1 pad K6: /1V8 -> /GND
- U1 pad K7: /1V8 -> /GND
- U1 pad K8: /1V8 -> /GND
- U1 pad K9: /1V8 -> /GND
- U1 pad L5: /1V8 -> /GND
- U1 pad L6: /1V8 -> /GND
- U1 pad M1: /1V8 -> /GND
- U1 pad N1: /1V8 -> /GND
- U1 pad N13: Net-(U1-PadN13) -> /MCU/SPI5_MISO
- U1 pad P13: Net-(U1-PadP13) -> /MCU/SPI5_SCK
- U1 pad P8: Net-(U1-PadP8) -> /MCU/SPI5_MOSI
- U2 pad A1: /1V8 -> /GND
- U2 pad A10: /FPGA/IO_3V3_6 -> /FPGA/IO_3V3_5
- U2 pad A11: /1V8 -> /GND
- U2 pad A12: /FPGA/IO_3V3_10 -> /FPGA/IO_3V3_9
- U2 pad A13: /FPGA/IO_3V3_13 -> /FPGA/IO_3V3_12
- U2 pad A14: /FPGA/IO_3V3_14 -> /FPGA/IO_3V3_13
- U2 pad A15: /FPGA/IO_3V3_18 -> /FPGA/IO_3V3_17
- U2 pad A8: /FPGA/IO_3V3_3 -> /FPGA/IO_3V3_2
- U2 pad A9: /FPGA/IO_3V3_4 -> /FPGA/IO_3V3_3
- U2 pad B10: /FPGA/IO_3V3_7 -> /FPGA/IO_3V3_6
- U2 pad B11: /FPGA/IO_3V3_8 -> /FPGA/IO_3V3_7
- U2 pad B12: /FPGA/IO_3V3_9 -> /FPGA/IO_3V3_8
- U2 pad B14: /FPGA/IO_3V3_16 -> /FPGA/IO_3V3_15
- U2 pad B15: /FPGA/IO_3V3_17 -> /FPGA/IO_3V3_16
- U2 pad B16: /FPGA/IO_3V3_20 -> /FPGA/IO_3V3_19
- U2 pad B8: /1V8 -> /GND
- U2 pad B9: /FPGA/IO_3V3_5 -> /FPGA/IO_3V3_4
- U2 pad C11: /FPGA/IO_3V3_21 -> /FPGA/CLK_3V3_0
- U2 pad C13: /FPGA/IO_3V3_23 -> /FPGA/IN_3V3_0_N
- U2 pad C14: /FPGA/IO_3V3_15 -> /FPGA/IO_3V3_14
- U2 pad C15: /1V8 -> /GND
- U2 pad C16: /FPGA/IO_3V3_19 -> /FPGA/IO_3V3_18
- U2 pad C5: /1V8 -> /GND
- U2 pad C8: /FPGA/IO_3V3_1 -> /PSU_TEMP
- U2 pad C9: /FPGA/IO_3V3_2 -> /FPGA/IO_3V3_1
- U2 pad D11: /FPGA/IO_3V3_26 -> /FPGA/IO_3V3_24
- U2 pad D12: /1V8 -> /GND
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
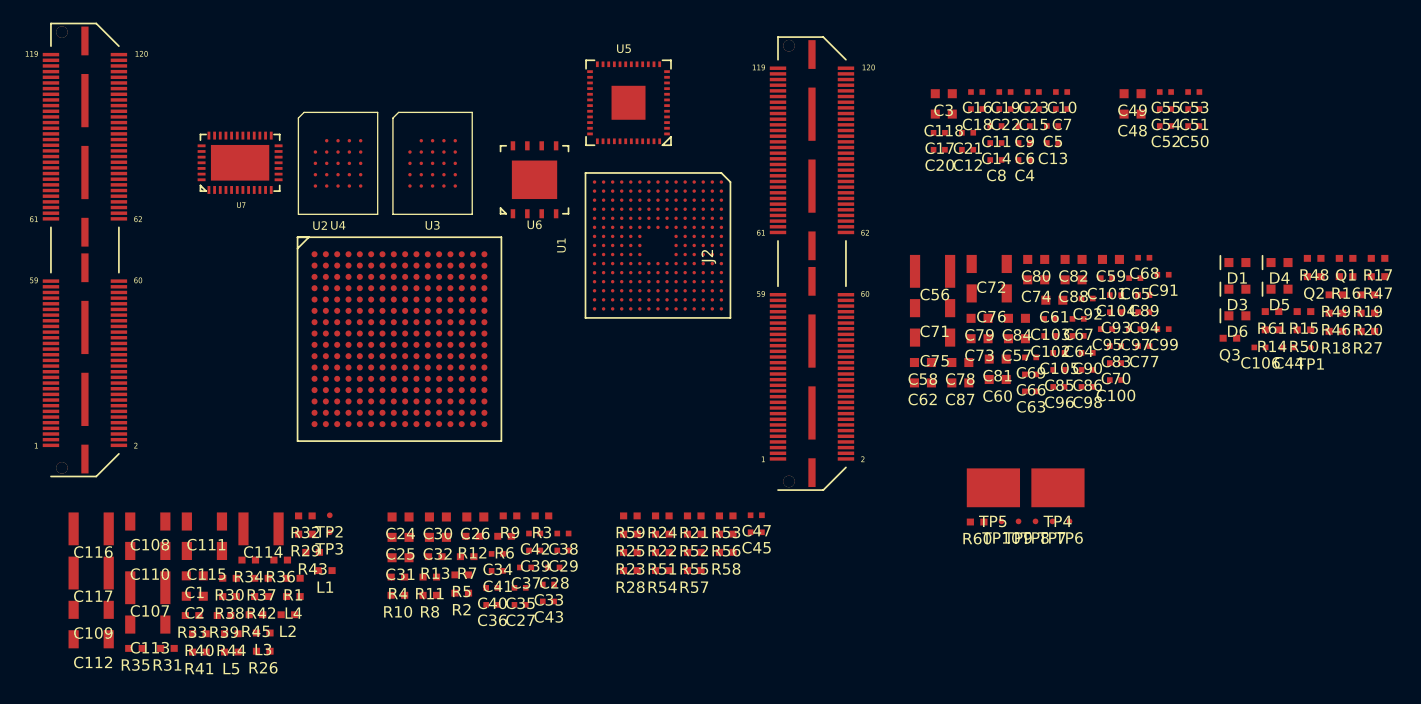
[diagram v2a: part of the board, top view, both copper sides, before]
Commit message: Assigned inductor footprints
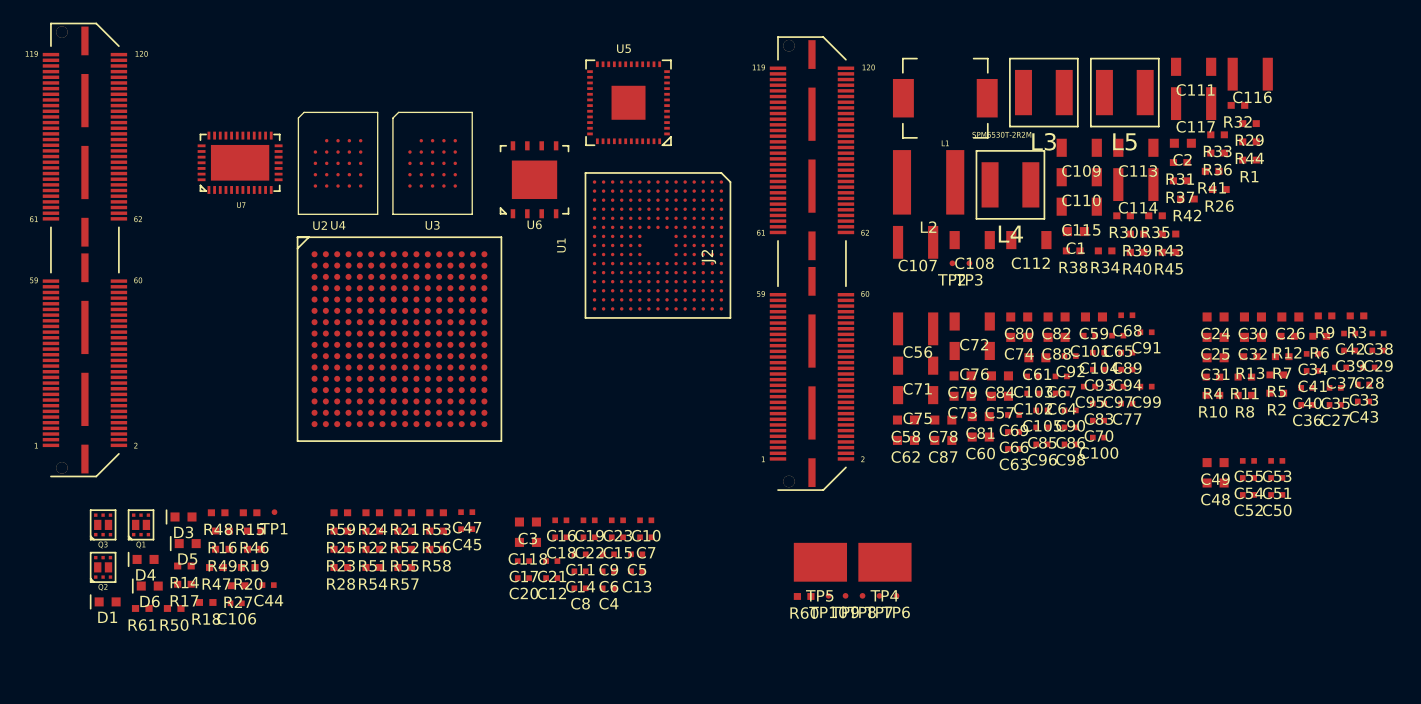
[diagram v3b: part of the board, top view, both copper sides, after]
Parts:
- L1: footprint azonenberg_pcb:EIA_0402_RES_NOSILK -> azonenberg_pcb:INDUCTOR_TDK_SPM6530
- L2: footprint azonenberg_pcb:EIA_0402_RES_NOSILK -> azonenberg_pcb:INDUCTOR_YUDEN_NR6028
- L3, L4, L5: footprint azonenberg_pcb:EIA_0402_RES_NOSILK -> azonenberg_pcb:INDUCTOR_YUDEN_NRS5030
- Q1, Q2, Q3: footprint azonenberg_pcb:EIA_0402_RES_NOSILK -> azonenberg_pcb:DFN_6_0.65MM_2x2MM_GDS
- moved Q2 110.0 mm to (29.4, 72.2)
- moved C116 109.9 mm to (130.7, 28.7)
- moved R17 109.3 mm to (36.6, 73.7)
- moved Q1 109.0 mm to (32.8, 68.5)
- moved C117 105.8 mm to (125.7, 31.3)
- moved R47 105.7 mm to (39.4, 72.2)
- moved D1 104.2 mm to (29.8, 75.3)
- moved D4 103.5 mm to (33.2, 71.5)
- moved R61 103.1 mm to (32.9, 75.9)
- moved R50 102.7 mm to (35.7, 75.9)
- moved R18 102.6 mm to (38.5, 75.3)
- moved R27 102.3 mm to (41.3, 73.8)
- moved R16 101.7 mm to (39.9, 69.0)
- moved R20 101.4 mm to (42.2, 72.2)
- moved R49 100.9 mm to (39.9, 70.6)
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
